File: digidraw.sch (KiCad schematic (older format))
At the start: 0 parts

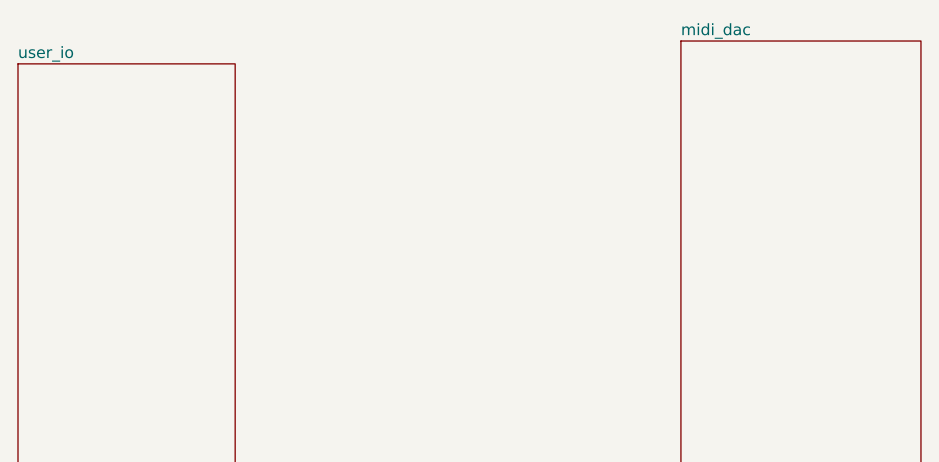
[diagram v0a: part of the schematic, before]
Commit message: Work on user io subsystem schematic
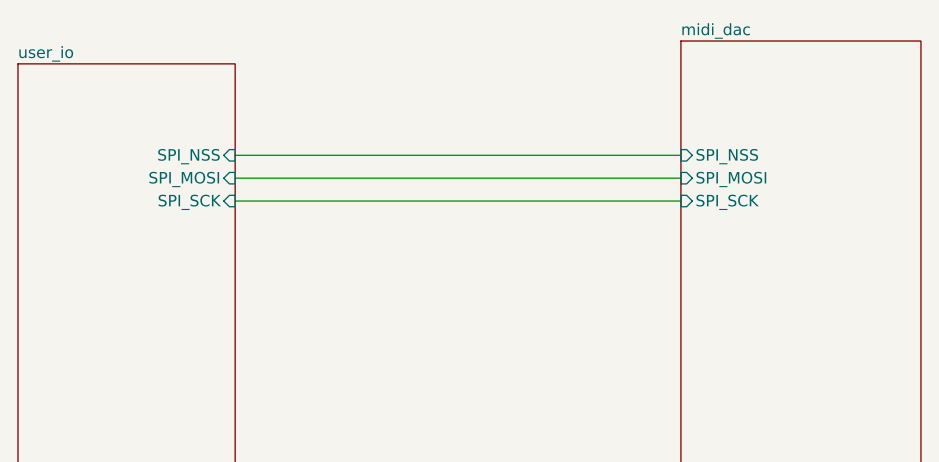
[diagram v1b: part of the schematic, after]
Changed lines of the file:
@@
 F0 "user_io" 50
 F1 "user_io.sch" 50
+F2 "SPI_MOSI" I R 4000 2950 50
+F3 "SPI_SCK" I R 4000 3050 50
+F4 "SPI_NSS" I R 4000 2850 50
 $EndSheet
 $Sheet
@@
 F0 "midi_dac" 50
 F1 "midi_dac.sch" 50
+F2 "SPI_MOSI" I L 5950 2950 50
+F3 "SPI_SCK" I L 5950 3050 50
+F4 "SPI_NSS" I L 5950 2850 50
 $EndSheet
+Wire Wire Line
+	4000 2850 5950 2850
+Wire Wire Line
+	4000 2950 5950 2950
+Wire Wire Line
+	4000 3050 5950 3050
 $EndSCHEMATC

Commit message: Add f4 decoupling capacitors, add dac, add power converter circuit
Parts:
- added C?: 100u, symbol Device:C_Small
- added C?: 100n, symbol Device:C_Small
- added C?: 10u, symbol Device:C_Small
- added J?: Barrel_Jack, symbol Connector:Barrel_Jack
- added R?: 470, symbol Device:R_Small
- added R?: 71.5, symbol Device:R_Small
- added R?: 330, symbol Device:R_Small
- added U?: LM317_TO3, Package_TO_SOT_THT:TO-3, symbol Regulator_Linear:LM317_TO3
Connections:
- net labels added: +3.3V, GND, VCC
- wire segments 3 -> 29
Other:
- note added: "Power Converter"
- note added: "Power In"
- note added: "Top Level & Power Circuit\n"

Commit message: Finish prototype of DAC/USB/Power system
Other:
- note added: "Version 1.0.0"
- moved on the sheet: C?, J?, R?, U?

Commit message: Add one more debug connector
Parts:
- added D?: RED_LED, symbol Device:LED
- added R?: 50, symbol Device:R_Small
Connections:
- wire segments 29 -> 32
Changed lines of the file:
@@
 Wire Notes Line
 	3750 2300 3750 3650
-Wire Notes Line
-	3750 3650 7000 3650
-Wire Notes Line
-	7000 3650 7000 2300
-Wire Notes Line
-	7000 2300 3750 2300
 Wire Wire Line
 	4800 4450 5600 4450
@@
 Text Notes 9850 7870 0    50   ~ 0
 Version 1.0.0
+$Comp
+L Device:LED D?
+U 1 1 604BBE37
+P 7150 3100
+F 0 "D?" V 7189 2982 50  0000 R CNN
+F 1 "RED_LED" V 7098 2982 50  0000 R CNN
+F 2 "" H 7150 3100 50  0001 C CNN
+F 3 "~" H 7150 3100 50  0001 C CNN
+	1    7150 3100
+	0    -1   -1   0
+$EndComp
+$Comp
+L Device:R_Small R?
+U 1 1 604BCA6D
+P 7150 2800
+F 0 "R?" H 7209 2846 50  0000 L CNN
+F 1 "50" H 7209 2755 50  0000 L CNN
+F 2 "" H 7150 2800 50  0001 C CNN
+F 3 "~" H 7150 2800 50  0001 C CNN
+	1    7150 2800
+	1    0    0    -1
+$EndComp
+Wire Wire Line
+	7150 2900 7150 2950
+$Comp
+L power:GND #PWR?
+U 1 1 604BE106
+P 7150 3300
+F 0 "#PWR?" H 7150 3050 50  0001 C CNN
+F 1 "GND" H 7155 3127 50  0000 C CNN
+F 2 "" H 7150 3300 50  0001 C CNN
+F 3 "" H 7150 3300 50  0001 C CNN
+	1    7150 3300
+	1    0    0    -1
+$EndComp
+Wire Wire Line
+	7150 3300 7150 3250
+$Comp
+L power:+3.3V #PWR?
+U 1 1 604BEBCA
+P 7150 2650
+F 0 "#PWR?" H 7150 2500 50  0001 C CNN
+F 1 "+3.3V" H 7165 2823 50  0000 C CNN
+F 2 "" H 7150 2650 50  0001 C CNN
+F 3 "" H 7150 2650 50  0001 C CNN
+	1    7150 2650
+	1    0    0    -1
+$EndComp
+Wire Wire Line
+	7150 2650 7150 2700
+Wire Notes Line
+	7600 2300 7600 3650
+Wire Notes Line
+	3750 3650 7600 3650
+Wire Notes Line
+	3750 2300 7600 2300
 $EndSCHEMATC

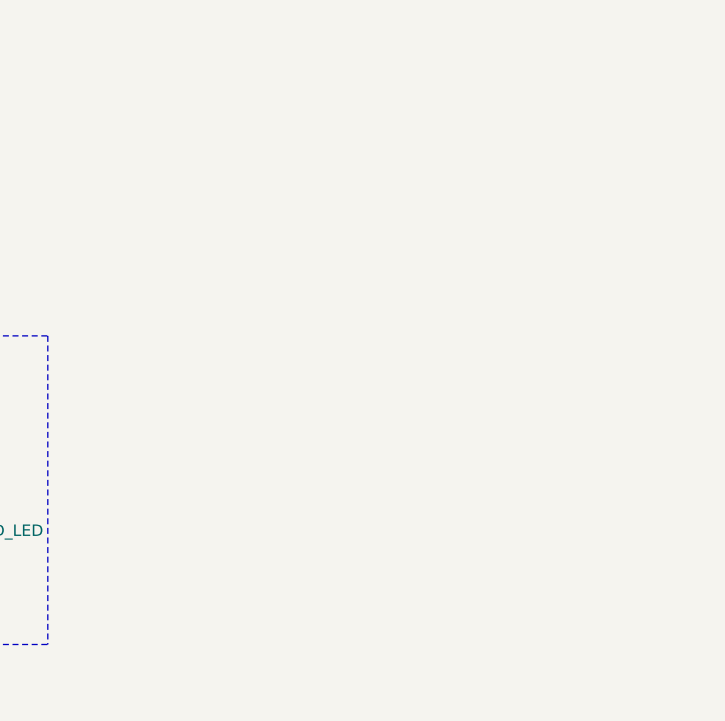
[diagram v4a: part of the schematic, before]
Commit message: Add mounting holes
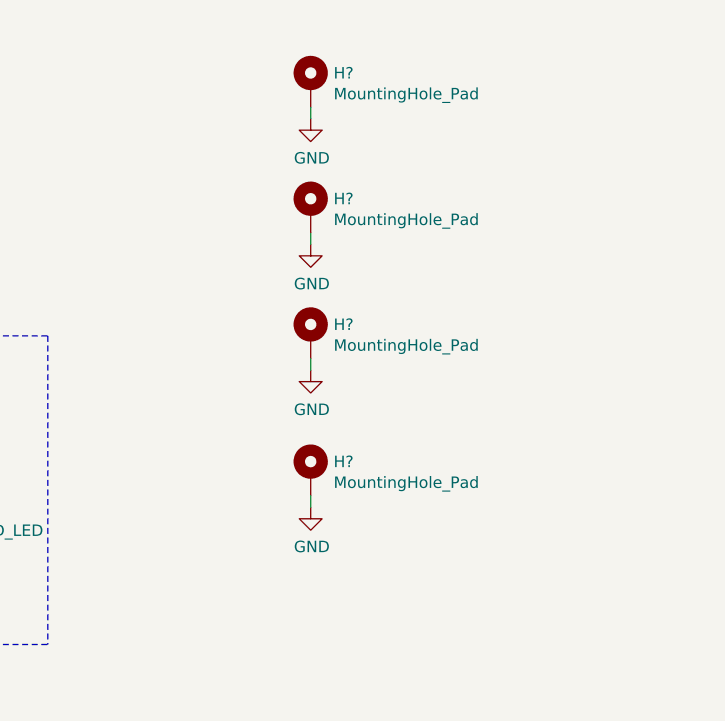
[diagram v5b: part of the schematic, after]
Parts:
- added H? (x4): MountingHole_Pad, symbol Mechanical:MountingHole_Pad
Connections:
- wire segments 32 -> 36
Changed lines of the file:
@@
 Wire Notes Line
 	3750 2300 7600 2300
+$Comp
+L Mechanical:MountingHole_Pad H?
+U 1 1 604BB9D1
+P 8750 1200
+F 0 "H?" H 8850 1249 50  0000 L CNN
+F 1 "MountingHole_Pad" H 8850 1158 50  0000 L CNN
+F 2 "" H 8750 1200 50  0001 C CNN
+F 3 "~" H 8750 1200 50  0001 C CNN
+	1    8750 1200
+	1    0    0    -1
+$EndComp
+$Comp
+L power:GND #PWR?
+U 1 1 604BC603
+P 8750 1350
+F 0 "#PWR?" H 8750 1100 50  0001 C CNN
+F 1 "GND" H 8755 1177 50  0000 C CNN
+F 2 "" H 8750 1350 50  0001 C CNN
+F 3 "" H 8750 1350 50  0001 C CNN
+	1    8750 1350
+	1    0    0    -1
+$EndComp
+Wire Wire Line
+	8750 1350 8750 1300
+$Comp
+L Mechanical:MountingHole_Pad H?
+U 1 1 604BDAEB
+P 8750 1750
+F 0 "H?" H 8850 1799 50  0000 L CNN
+F 1 "MountingHole_Pad" H 8850 1708 50  0000 L CNN
+F 2 "" H 8750 1750 50  0001 C CNN
+F 3 "~" H 8750 1750 50  0001 C CNN
+	1    8750 1750
+	1    0    0    -1
+$EndComp
+$Comp
+L power:GND #PWR?
+U 1 1 604BDB89
+P 8750 1900
+F 0 "#PWR?" H 8750 1650 50  0001 C CNN
+F 1 "GND" H 8755 1727 50  0000 C CNN
+F 2 "" H 8750 1900 50  0001 C CNN
+F 3 "" H 8750 1900 50  0001 C CNN
+	1    8750 1900
+	1    0    0    -1
+$EndComp
+Wire Wire Line
+	8750 1900 8750 1850
+$Comp
+L Mechanical:MountingHole_Pad H?
+U 1 1 604C1699
+P 8750 2300
+F 0 "H?" H 8850 2349 50  0000 L CNN
+F 1 "MountingHole_Pad" H 8850 2258 50  0000 L CNN
+F 2 "" H 8750 2300 50  0001 C CNN
+F 3 "~" H 8750 2300 50  0001 C CNN
+	1    8750 2300
+	1    0    0    -1
+$EndComp
+$Comp
+L power:GND #PWR?
+U 1 1 604C169F
+P 8750 2450
+F 0 "#PWR?" H 8750 2200 50  0001 C CNN
+F 1 "GND" H 8755 2277 50  0000 C CNN
+F 2 "" H 8750 2450 50  0001 C CNN
+F 3 "" H 8750 2450 50  0001 C CNN
+	1    8750 2450
+	1    0    0    -1
+$EndComp
+Wire Wire Line
+	8750 2450 8750 2400
+$Comp
+L Mechanical:MountingHole_Pad H?
+U 1 1 604C2385
+P 8750 2900
+F 0 "H?" H 8850 2949 50  0000 L CNN
+F 1 "MountingHole_Pad" H 8850 2858 50  0000 L CNN
+F 2 "" H 8750 2900 50  0001 C CNN
+F 3 "~" H 8750 2900 50  0001 C CNN
+	1    8750 2900
+	1    0    0    -1
+$EndComp
+$Comp
+L power:GND #PWR?
+U 1 1 604C238B
+P 8750 3050
+F 0 "#PWR?" H 8750 2800 50  0001 C CNN
+F 1 "GND" H 8755 2877 50  0000 C CNN
+F 2 "" H 8750 3050 50  0001 C CNN
+F 3 "" H 8750 3050 50  0001 C CNN
+	1    8750 3050
+	1    0    0    -1
+$EndComp
+Wire Wire Line
+	8750 3050 8750 3000
 $EndSCHEMATC

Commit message: Make updates per suggestions
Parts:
- removed R?: 470, symbol Device:R_Small
- removed R?: 71.5, symbol Device:R_Small
- added C4, C6: 10u, symbol Device:C_Small
- added C5: 100n, symbol Device:C_Small
- added F1: 1.5, symbol Device:Fuse_Small
- added F2: 50m, symbol Device:Fuse_Small
- added J1: USB_B_Micro, symbol Connector:USB_B_Micro
- added R1, R9: 542, symbol Device:R_Small
- added R10: 330, symbol Device:R_Small
- added R3, R8: 0, symbol Device:R_Small
- added R4, R5, R6: 10k, symbol Device:R_Small
- added U2: LM317_TO3, Package_TO_SOT_THT:TO-3, symbol Regulator_Linear:LM317_TO3
- C1: renamed from C?; value 100u -> 10u
- gave numbers to parts that had none: 11
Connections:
- net labels added: +3.3VADC, +5V
- net labels removed: VCC
- wire segments 36 -> 83
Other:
- note added: "Not Connected"
- note added: "Version 2.0.0"
- note removed: "Version 1.0.0"
- moved on the sheet: C1, C2, C3, D1, H1, H2, H3, H4, J2, R2, R7, U1

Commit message: Update power supply system
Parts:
- removed D1: RED_LED, symbol Device:LED
- removed F2: 50m, symbol Device:Fuse_Small
- removed U1: LM317_TO3, Package_TO_SOT_THT:TO-3, symbol Regulator_Linear:LM317_TO3
- added C48, C49, C50: 22u, symbol Device:C_Small
- added C51, C52, C55, C56: 10u, symbol Device:C_Small
- added C53, C54: 100n, symbol Device:C_Small
- added D1: SMAJ20CA-13-F, symbol Device:D_TVS
- added D6: 9.1, symbol Device:D_Zener_Small
- added L1: 1.5u, symbol Device:L_Small
- added M1: FQP47P06, symbol pspice:MPMOS
- added R47, R48: 542, symbol Device:R_Small
- added R49: 0, symbol Device:R_Small
- added R50, R51: 330, symbol Device:R_Small
- added U1: TPS63070RNMR, Texas_Instruments-RNM0015A-0-0-*, symbol TI_REGULATOR:TPS63070RNMR
- added U8: LM117_TO3, Package_TO_SOT_THT:TO-3, symbol Regulator_Linear:LM117_TO3
- C1: value 10u -> 1u
- C2: value 100n -> 10u
- F1: value 1.5 -> 3
- R1: value 542 -> 100k
- R10: value 330 -> 100k
- R2: value 330 -> 10k
- R7: value 50 -> 605k
- R9: value 542 -> 110k
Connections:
- net +3V3: now also U2.3 (VO), C53.1, C55.1, R50.2; no longer C2.1, C3.1, R2.1, R7.1
- net +5V: now also R49.1; no longer F1.1, R3.1, R8.1
- net GND: now also R9.2, C48.2, C49.2, C50.2, C51.2, C52.2, C53.2, C54.2, C55.2, C56.2, D1.2 (A2), R47.2, R48.2, U1.10 (PGND), U1.15 (VSEL), U1.4 (GND); no longer R9.1
- net at R1.1: now also D6.2 (A), M1.2 (G); no longer R2.2
- net at C1.1, F1.2: now also D1.1 (A1), M1.1 (D)
- net at R7.2: now also R9.1, U1.5 (FB)
- net at C4.1: now also C2.1, C3.1, R2.1, D6.1 (K), M1.3 (S), M1.4 (B), U1.12-13 (VIN); no longer U2.2 (VI)
- net +3.3VADC: no longer names the net of C6.1, R10.1
- net +3.3VADC: now also R7.1, U2.2 (VI), C48.1, C49.1, C50.1, C51.1, C52.1, R49.2, U1.7-8 (VOUT), U8.2 (VI); no longer C5.1, U2.3 (VO)
- new net: R2.2, U1.1 (PS/S), U1.14 (EN)
- new net: L1.2, U1.11 (L1)
- new net: R10.2, U1.2 (PG)
- new net: C5.1, U1.3 (VAUX)
- new net: L1.1, U1.9 (L2)
- new net: R48.1, R51.1, U8.1 (ADJ)
- new net: R47.1, R50.1, U2.1 (ADJ)
- new net +3.3VDAC: C54.1, C56.1, R51.2, U8.3 (VO)
- new net VIN: F1.1, R3.1, R8.1
- no-connect marks 0 -> 1
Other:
- note added: "As close as possible to power\n0603 footprint"
- note added: "DAC"
- note added: "Power Supply Circuitry\n"
- note added: "USB VBus"
- note added: "VDD\n"
- note removed: "Power Converter"
- moved on the sheet: H1, H2, H3, H4

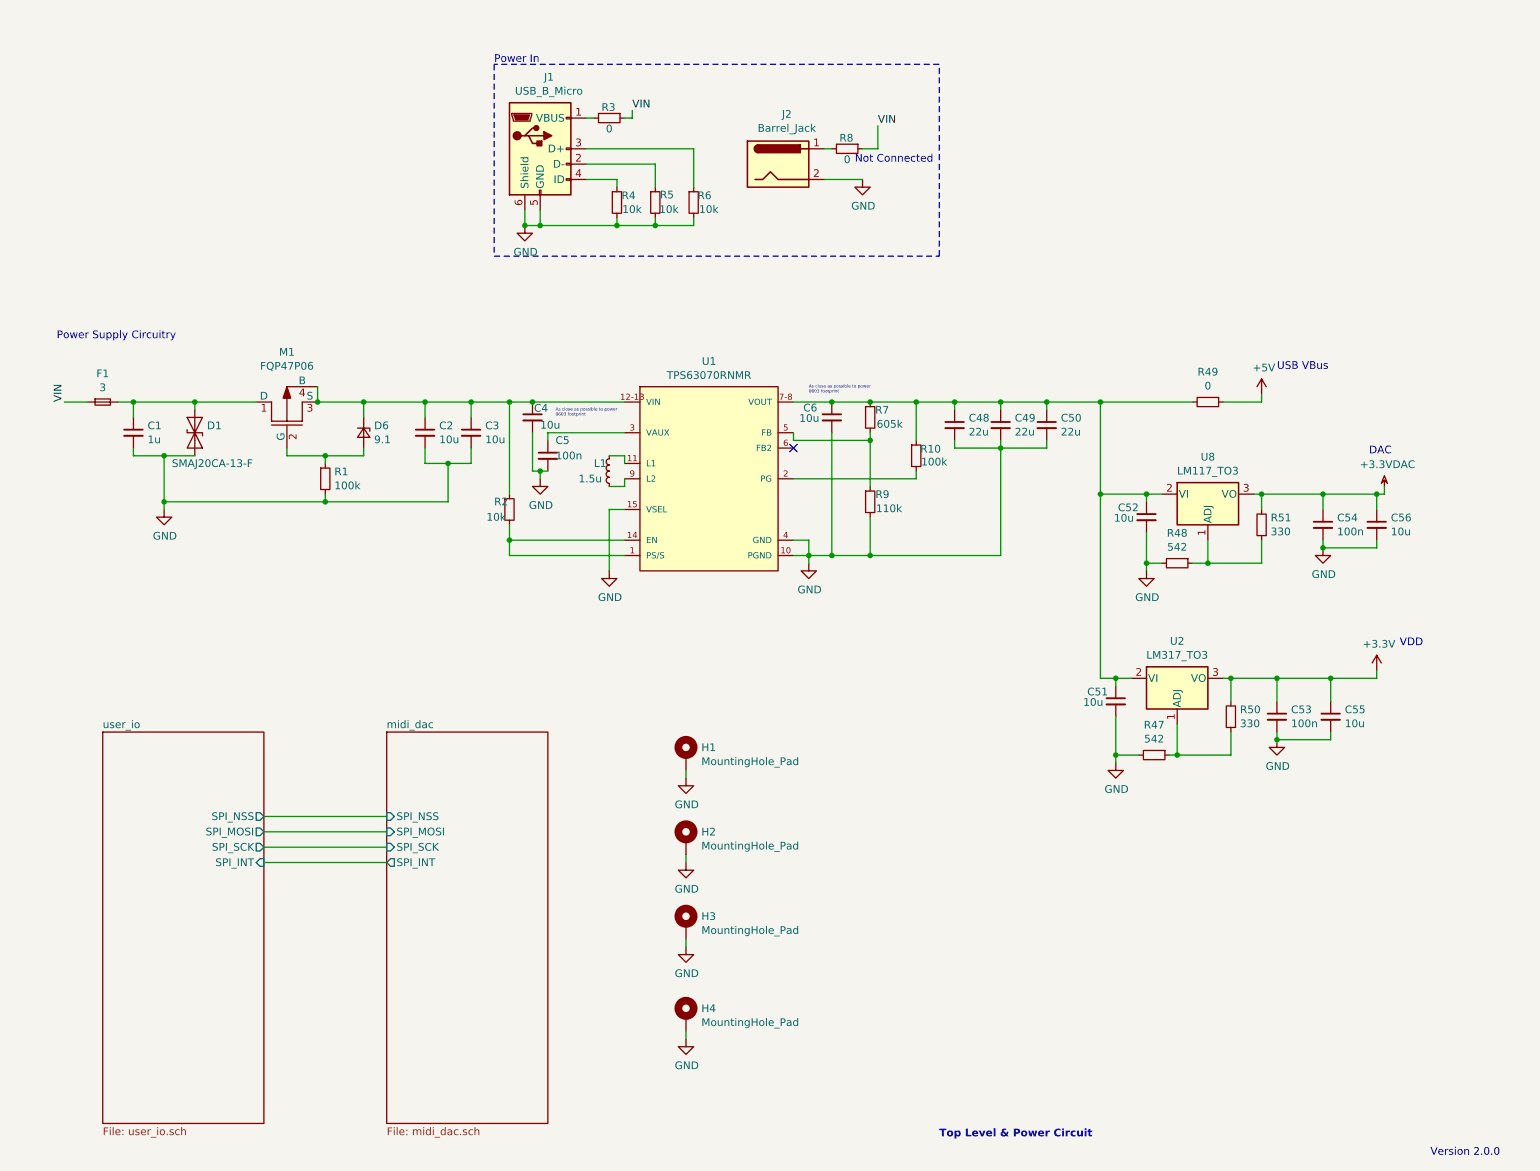
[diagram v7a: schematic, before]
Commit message: Final iteration before pcb design review
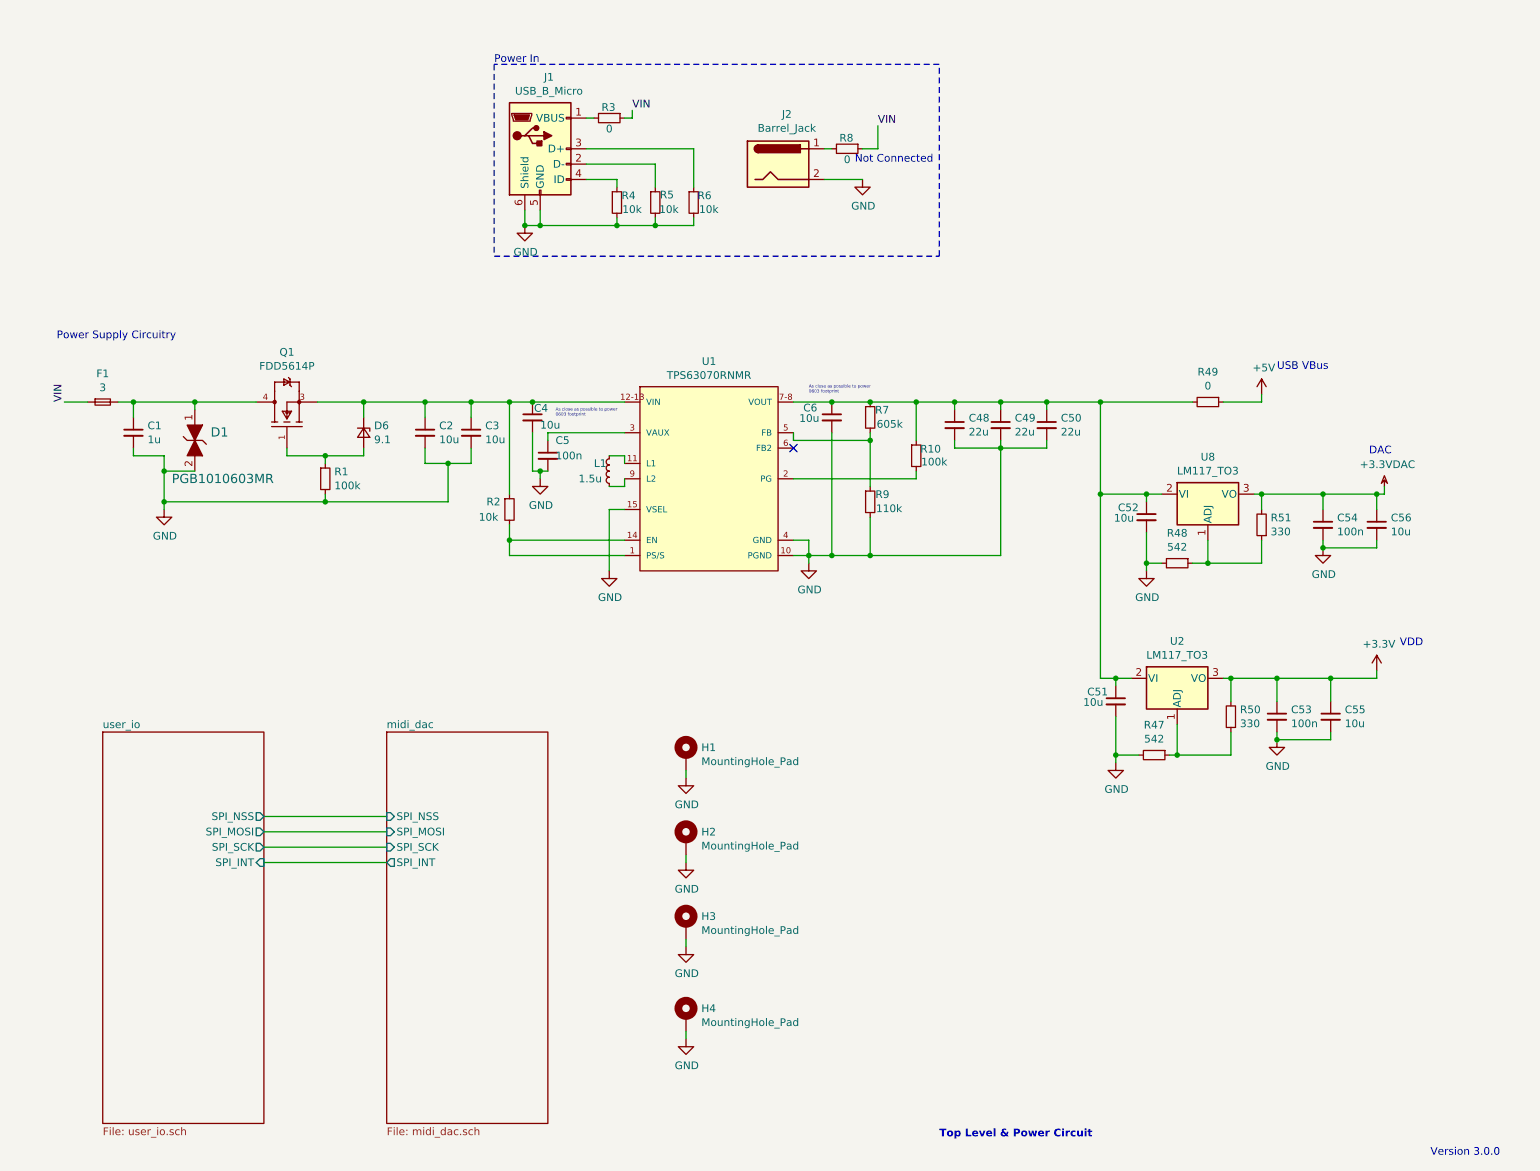
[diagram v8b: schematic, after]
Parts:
- removed D1: SMAJ20CA-13-F, symbol Device:D_TVS
- removed M1: FQP47P06, symbol pspice:MPMOS
- removed U2: LM317_TO3, Package_TO_SOT_THT:TO-3, symbol Regulator_Linear:LM317_TO3
- added D1: PGB1010603MR, digikey-footprints:0603, symbol dk_TVS-Diodes:PGB1010603MR
- added Q1: FDD5614P, MOSFET_TI:ON_Semi-369AS-09_2016-O-0, symbol FDD5614P:FDD5614P
- added U2: LM117_TO3, Package_TO_SOT_THT:TO-3, symbol Regulator_Linear:LM117_TO3
- C1, C2, C3, C48, C49, C5, C50, C51, C52, C53, C54: footprint (none) -> Capacitor_SMD:C_0805_2012Metric
- C4, C55, C56, C6: footprint (none) -> Capacitor_SMD:C_0603_1608Metric
- D6: footprint (none) -> Diode_SMD:D_0603_1608Metric
- F1: footprint (none) -> Fuse:Fuse_0805_2012Metric
- H1, H2, H3, H4: footprint (none) -> MountingHole:MountingHole_4.3mm_M4_Pad_Via
- J1: footprint (none) -> Connector_USB:USB_Micro-B_Molex-105017-0001
- J2: footprint (none) -> digikey-footprints:Barrel_Jack_5.5mmODx2.1mmID_PJ-202A
- L1: footprint (none) -> Inductor_SMD:L_0603_1608Metric
- R1, R10, R2, R3, R4, R47, R48, R49, R5, R50, R51, R6, R7, R8, R9: footprint (none) -> Resistor_SMD:R_0603_1608Metric
- U1: footprint Texas_Instruments-RNM0015A-0-0-* -> TI_REG:Texas_Instruments-RNM0015A-0-0-MFG
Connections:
- net +3V3: now also U2.3 (VO)
- net GND: now also D1.2
- net at C1.1, F1.2: now also D1.1, Q1.4 (D)
- net at D6.2 (A), R1.1: now also Q1.1 (G)
- net at C2.1, C3.1, C4.1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: now also Q1.3 (S)
- net at C48.1, C49.1, C50.1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: now also U2.2 (VI)
- net at R47.1, R50.1: now also U2.1 (ADJ)
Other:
- note added: "Version 3.0.0"
- note removed: "Version 2.0.0"
